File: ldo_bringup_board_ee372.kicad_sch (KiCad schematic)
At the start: 75 parts, among them J1 VIN, J10 MD_SW_EN, J13 VSIG, J14 VSIG_BUF, J2 GND, J3 IBIAS, J4 VOUT, J5 VIN_SMA, J6 VOUT_SMA, J7 GND, J8 5V, Q1 FDV305N, Q2 FDV305N, Q3 FDV305N, Q4 FDV305N, Q5 FDV305N, SW1 SW_SPDT, U1 LDO_DualMode_BGR_EE372

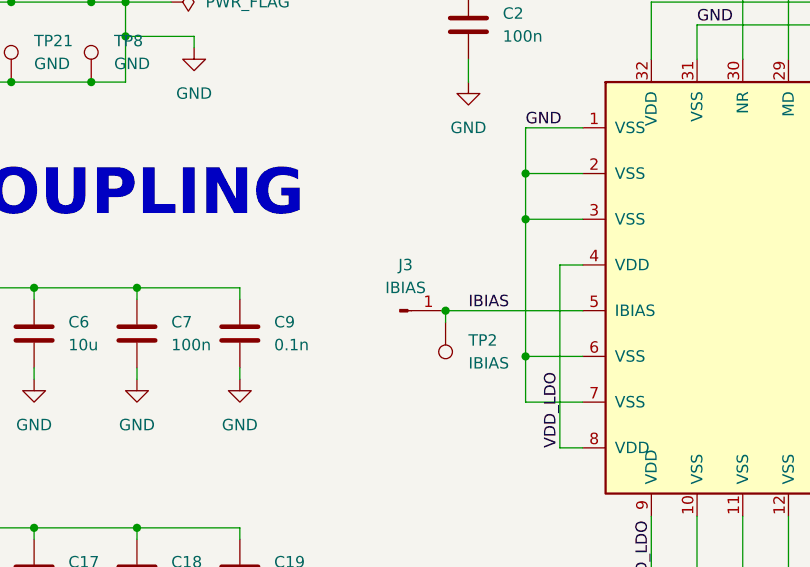
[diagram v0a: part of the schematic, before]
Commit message: Monitor VDD, VDD_LDO, VOUT_LDO and VOUT on Teensy ADC pins through 10k
R45 to R48 connect Teensy pins 20, 19, 18 and 17 (A6, A5, A4, A3) to the
four rail nets. The 10k limits current if the Teensy is unpowered while
the chip is on. NR, IBIAS and MD stay off the Teensy.
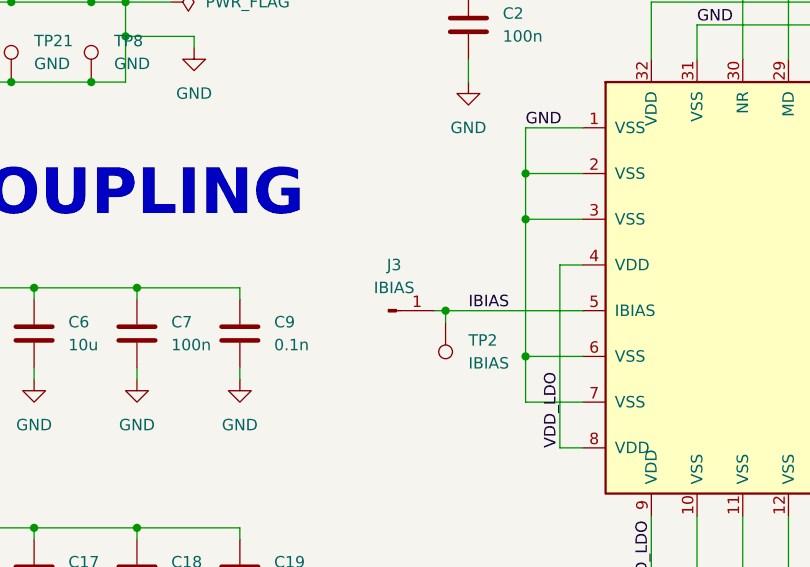
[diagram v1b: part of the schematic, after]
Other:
- moved on the sheet: J3
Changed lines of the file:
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@@
 	(wire
 		(pts
+			(xy 81.28 153.67) (xy 82.55 153.67)
+		)
+		(stroke
+			(width 0)
+			(type default)
+		)
+	)
+	(wire
+		(pts
 			(xy 224.79 143.51) (xy 224.79 144.78)
 		)
@@
 	(symbol
 		(lib_id "Connector:Conn_01x01_Pin")
-		(at 77.47 153.67 0)
+		(at 76.2 153.67 0)
 		(unit 1)
 		(body_style 1)
@@
 		(dnp no)
 		(property "Reference" "J3"
-			(at 78.105 148.59 0)
+			(at 76.835 148.59 0)
 			(show_name no)
 			(do_not_autoplace no)
@@
 		)
 		(property "Value" "IBIAS"
-			(at 78.105 151.13 0)
+			(at 76.835 151.13 0)
 			(show_name no)
 			(do_not_autoplace no)
@@
 		)
 		(property "Footprint" "ldo_bringup_board_ee372:CalTest_CT3151SP"
-			(at 77.47 153.67 0)
+			(at 76.2 153.67 0)
 			(hide yes)
 			(show_name no)
@@
 		)
 		(property "Datasheet" "https://mm.digikey.com/Volume0/opasdata/d220001/medias/docus/4846/DS_1768_Catalog.pdf"
-			(at 77.47 153.67 0)
+			(at 76.2 153.67 0)
 			(hide yes)
 			(show_name no)
@@
 		)
 		(property "Description" "CONN BANANA JACK SOLDER WHITE"
-			(at 77.47 153.67 0)
+			(at 76.2 153.67 0)
 			(hide yes)
 			(show_name no)
@@
 		)
 		(property "Manufacturer" "Cal Test Electronics"
-			(at 77.47 153.67 0)
+			(at 76.2 153.67 0)
 			(hide yes)
 			(show_name no)
@@
 		)
 		(property "Manufacturer Part Number" "CT3151SP-9"
-			(at 77.47 153.67 0)
+			(at 76.2 153.67 0)
 			(hide yes)
 			(show_name no)
@@
 		)
 		(property "Distributer Link 1" "https://www.digikey.com/en/products/detail/cal-test-electronics/CT3151SP-9/6005550"
-			(at 77.47 153.67 0)
+			(at 76.2 153.67 0)
 			(hide yes)
 			(show_name no)

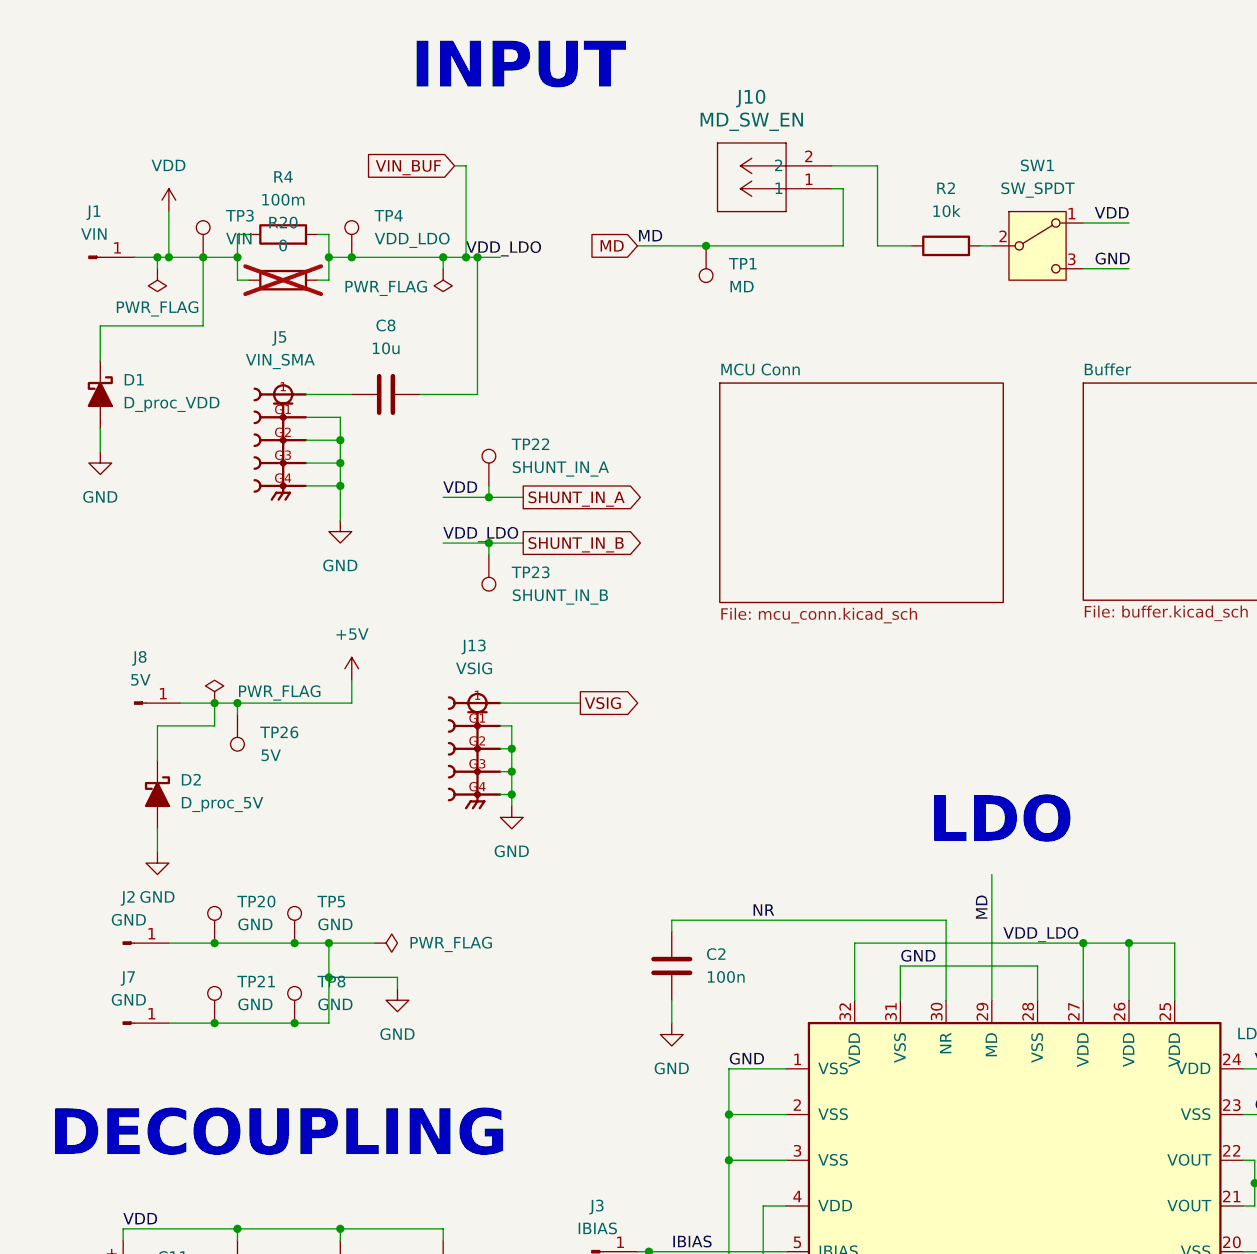
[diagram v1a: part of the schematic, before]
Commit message: Change noise amp feedback to 9k and outputs to 0 ohm, add NR jack and test point
Noise amplifier sheet:
- R16, R35, R38 changed from 10k to 9k
- R39, R40 (49.9 ohm) removed; R49, R50 (0 ohm) placed between the U5
  stage outputs and C36, C37
- J16, J17 values renamed NOISE_X100 and NOISE_X1000

Top sheet:
- TP30 added on NR
- J15 banana jack added, joined to NR through R39 (0 ohm, DNP)
- SW1 value renamed MD_SW
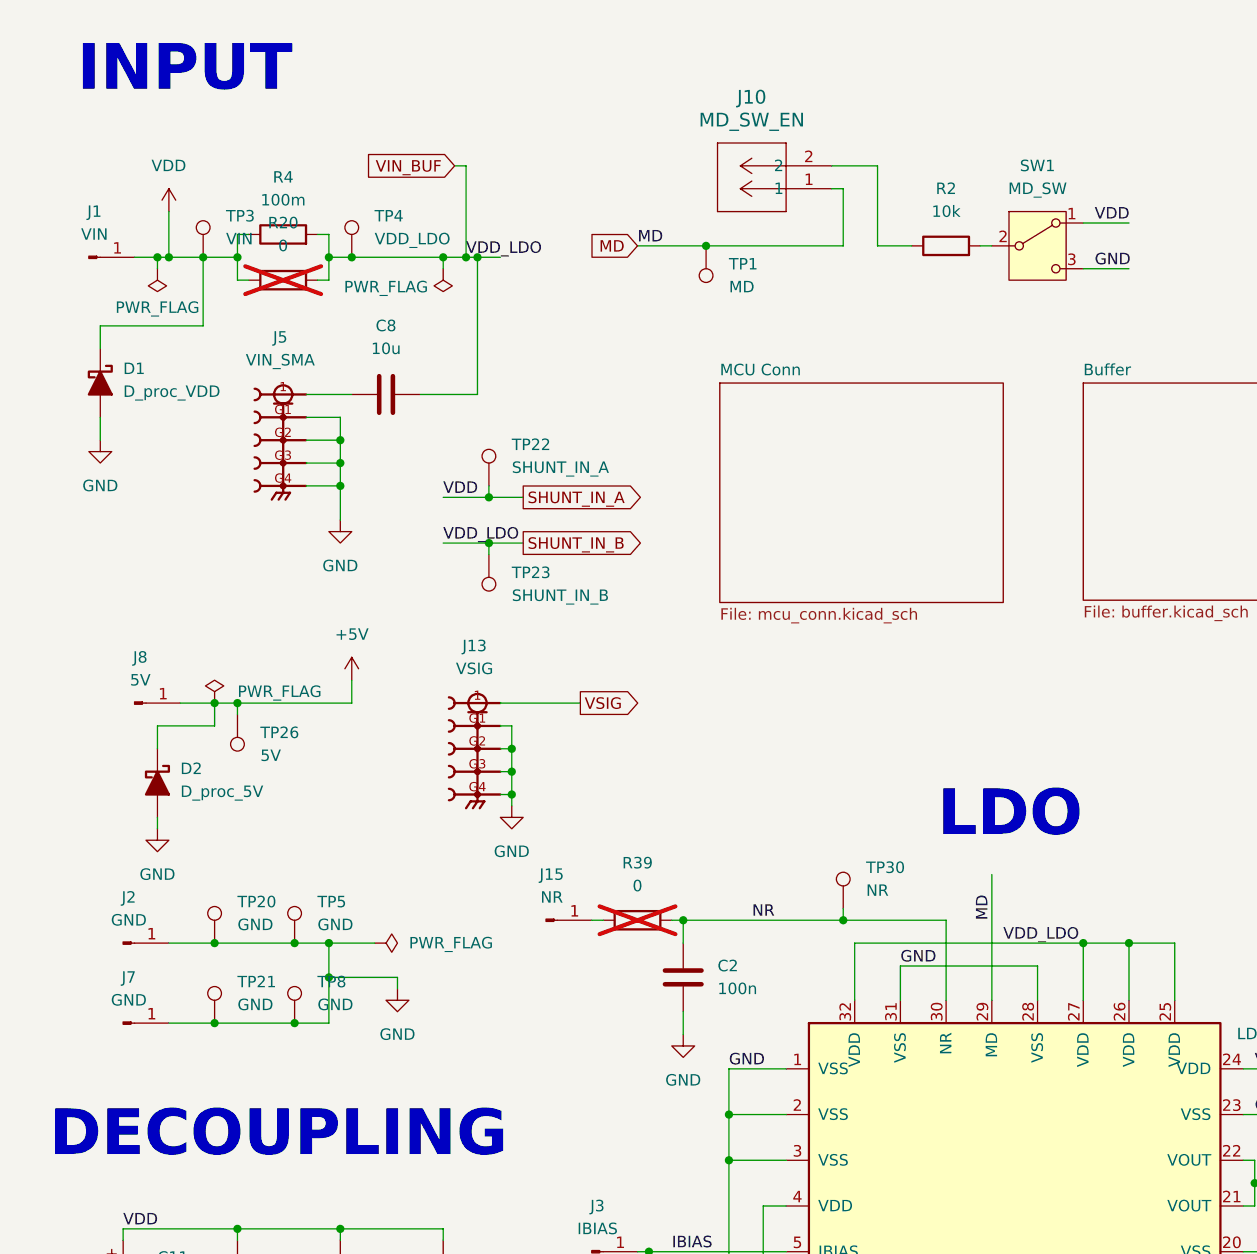
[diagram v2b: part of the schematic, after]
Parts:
- added J15: NR, ldo_bringup_board_ee372:CalTest_CT3151SP, symbol Connector:Conn_01x01_Pin
- added R39: 0, Resistor_SMD:R_0805_2012Metric_Pad1.20x1.40mm_HandSolder, symbol Device:R
- added TP30: NR, TestPoint:TestPoint_Keystone_5005-5009_Compact, symbol Connector:TestPoint
- SW1: value SW_SPDT -> MD_SW
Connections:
- net NR: now also R39.2, TP30.1
- new net: J15.1 (Pin_1), R39.1
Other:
- moved on the sheet: C2, D1, D2

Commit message: Modified some resistor footprints
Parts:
- R10, R11, R12, R13, R14, R5, R6, R7, R8, R9: footprint Resistor_SMD:R_0805_2012Metric_Pad1.20x1.40mm_HandSolder -> Resistor_SMD:R_0603_1608Metric_Pad0.98x0.95mm_HandSolder
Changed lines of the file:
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@@
 			)
 		)
-		(property "Footprint" "Resistor_SMD:R_0805_2012Metric_Pad1.20x1.40mm_HandSolder"
+		(property "Footprint" "Resistor_SMD:R_0603_1608Metric_Pad0.98x0.95mm_HandSolder"
 			(at 178.562 102.87 90)
 			(hide yes)
@@
 			)
 		)
-		(property "Footprint" "Resistor_SMD:R_0805_2012Metric_Pad1.20x1.40mm_HandSolder"
+		(property "Footprint" "Resistor_SMD:R_0603_1608Metric_Pad0.98x0.95mm_HandSolder"
 			(at 220.472 102.87 90)
 			(hide yes)
@@
 			)
 		)
-		(property "Footprint" "Resistor_SMD:R_0805_2012Metric_Pad1.20x1.40mm_HandSolder"
+		(property "Footprint" "Resistor_SMD:R_0603_1608Metric_Pad0.98x0.95mm_HandSolder"
 			(at 212.852 148.59 90)
 			(hide yes)
@@
 			)
 		)
-		(property "Footprint" "Resistor_SMD:R_0805_2012Metric_Pad1.20x1.40mm_HandSolder"
+		(property "Footprint" "Resistor_SMD:R_0603_1608Metric_Pad0.98x0.95mm_HandSolder"
 			(at 200.152 102.87 90)
 			(hide yes)
@@
 			)
 		)
-		(property "Footprint" "Resistor_SMD:R_0805_2012Metric_Pad1.20x1.40mm_HandSolder"
+		(property "Footprint" "Resistor_SMD:R_0603_1608Metric_Pad0.98x0.95mm_HandSolder"
 			(at 200.152 148.59 90)
 			(hide yes)
@@
 			)
 		)
-		(property "Footprint" "Resistor_SMD:R_0805_2012Metric_Pad1.20x1.40mm_HandSolder"
+		(property "Footprint" "Resistor_SMD:R_0603_1608Metric_Pad0.98x0.95mm_HandSolder"
 			(at 266.192 102.87 90)
 			(hide yes)
@@
 			)
 		)
-		(property "Footprint" "Resistor_SMD:R_0805_2012Metric_Pad1.20x1.40mm_HandSolder"
+		(property "Footprint" "Resistor_SMD:R_0603_1608Metric_Pad0.98x0.95mm_HandSolder"
 			(at 248.412 148.59 90)
 			(hide yes)
@@
 			)
 		)
-		(property "Footprint" "Resistor_SMD:R_0805_2012Metric_Pad1.20x1.40mm_HandSolder"
+		(property "Footprint" "Resistor_SMD:R_0603_1608Metric_Pad0.98x0.95mm_HandSolder"
 			(at 243.332 102.87 90)
 			(hide yes)
@@
 			)
 		)
-		(property "Footprint" "Resistor_SMD:R_0805_2012Metric_Pad1.20x1.40mm_HandSolder"
+		(property "Footprint" "Resistor_SMD:R_0603_1608Metric_Pad0.98x0.95mm_HandSolder"
 			(at 223.012 148.59 90)
 			(hide yes)
@@
 			)
 		)
-		(property "Footprint" "Resistor_SMD:R_0805_2012Metric_Pad1.20x1.40mm_HandSolder"
+		(property "Footprint" "Resistor_SMD:R_0603_1608Metric_Pad0.98x0.95mm_HandSolder"
 			(at 235.712 148.59 90)
 			(hide yes)

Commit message: Standardized resistor footprints
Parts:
- R2, R4: footprint Resistor_SMD:R_0805_2012Metric_Pad1.20x1.40mm_HandSolder -> Resistor_SMD:R_0603_1608Metric_Pad0.98x0.95mm_HandSolder
- renumbered R3 to RResistor_SMD:R_0603_1608Metric_Pad0.98x0.95mm_HandSolder
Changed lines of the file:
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@@
 			)
 		)
-		(property "Footprint" "Resistor_SMD:R_0805_2012Metric_Pad1.20x1.40mm_HandSolder"
+		(property "Footprint" "Resistor_SMD:R_0603_1608Metric_Pad0.98x0.95mm_HandSolder"
 			(at 41.91 42.418 90)
 			(hide yes)
@@
 		(dnp no)
 		(fields_autoplaced yes)
-		(property "Reference" "R3"
+		(property "Reference" "RResistor_SMD:R_0603_1608Metric_Pad0.98x0.95mm_HandSolder"
 			(at 242.57 30.48 90)
 			(show_name no)
@@
 			(project "ldo_bringup_board_ee372"
 				(path "/d41ff68c-d87d-4b82-b500-4ee675d17cf6"
-					(reference "R3")
+					(reference "RResistor_SMD:R_0603_1608Metric_Pad0.98x0.95mm_HandSolder")
 					(unit 1)
 				)
@@
 			)
 		)
-		(property "Footprint" "Resistor_SMD:R_0805_2012Metric_Pad1.20x1.40mm_HandSolder"
+		(property "Footprint" "Resistor_SMD:R_0603_1608Metric_Pad0.98x0.95mm_HandSolder"
 			(at 115.57 43.688 90)
 			(hide yes)

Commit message: placemtn and some schematic chagnes but might need to fix
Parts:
- removed C10: 10u, Capacitor_SMD:C_1206_3216Metric_Pad1.33x1.80mm_HandSolder, symbol Device:C
- R10, R11, R12, R13, R14, R2, R4, R5, R6, R7, R8, R9: footprint Resistor_SMD:R_0603_1608Metric_Pad0.98x0.95mm_HandSolder -> Resistor_SMD:R_0805_2012Metric_Pad1.20x1.40mm_HandSolder
- renumbered RResistor_SMD:R_0603_1608Metric_Pad0.98x0.95mm_HandSolder to R3
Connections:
- net SHUNT_OUT_B: now also J6.1
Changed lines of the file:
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@@
 	)
 	(junction
-		(at 227.33 54.61)
-		(diameter 0)
-		(color 0 0 0 0)
-	)
-	(junction
 		(at 212.09 128.27)
 		(diameter 0)
@@
 	(wire
 		(pts
-			(xy 243.84 54.61) (xy 260.35 54.61)
-		)
-		(stroke
-			(width 0)
-			(type default)
-		)
-	)
-	(wire
-		(pts
 			(xy 115.57 116.84) (xy 115.57 125.73)
 		)
@@
 	(wire
 		(pts
+			(xy 255.27 54.61) (xy 260.35 54.61)
+		)
+		(stroke
+			(width 0)
+			(type default)
+		)
+	)
+	(wire
+		(pts
 			(xy 110.49 121.92) (xy 125.73 121.92)
 		)
@@
 	(wire
 		(pts
+			(xy 255.27 39.37) (xy 255.27 54.61)
+		)
+		(stroke
+			(width 0)
+			(type default)
+		)
+	)
+	(wire
+		(pts
 			(xy 237.49 143.51) (xy 237.49 144.78)
 		)
@@
 	(wire
 		(pts
-			(xy 227.33 54.61) (xy 236.22 54.61)
-		)
-		(stroke
-			(width 0)
-			(type default)
-		)
-	)
-	(wire
-		(pts
 			(xy 29.21 128.27) (xy 34.29 128.27)
 		)
@@
 			)
 		)
-		(property "Footprint" "Resistor_SMD:R_0603_1608Metric_Pad0.98x0.95mm_HandSolder"
+		(property "Footprint" "Resistor_SMD:R_0805_2012Metric_Pad1.20x1.40mm_HandSolder"
 			(at 178.562 102.87 90)
 			(hide yes)
@@
 			)
 		)
-		(property "Footprint" "Resistor_SMD:R_0603_1608Metric_Pad0.98x0.95mm_HandSolder"
+		(property "Footprint" "Resistor_SMD:R_0805_2012Metric_Pad1.20x1.40mm_HandSolder"
 			(at 41.91 42.418 90)
 			(hide yes)
@@
 			)
 		)
-		(property "Footprint" "Resistor_SMD:R_0603_1608Metric_Pad0.98x0.95mm_HandSolder"
+		(property "Footprint" "Resistor_SMD:R_0805_2012Metric_Pad1.20x1.40mm_HandSolder"
 			(at 220.472 102.87 90)
 			(hide yes)
@@
 			)
 		)
-		(property "Footprint" "Resistor_SMD:R_0603_1608Metric_Pad0.98x0.95mm_HandSolder"
+		(property "Footprint" "Resistor_SMD:R_0805_2012Metric_Pad1.20x1.40mm_HandSolder"
 			(at 212.852 148.59 90)
 			(hide yes)
@@
 			)
 		)
-		(property "Footprint" "Resistor_SMD:R_0603_1608Metric_Pad0.98x0.95mm_HandSolder"
+		(property "Footprint" "Resistor_SMD:R_0805_2012Metric_Pad1.20x1.40mm_HandSolder"
 			(at 200.152 102.87 90)
 			(hide yes)
@@
 	)
 	(symbol
-		(lib_id "Device:C")
-		(at 240.03 54.61 90)
-		(unit 1)
-		(body_style 1)
-		(exclude_from_sim no)
-		(in_bom yes)
-		(on_board yes)
-		(in_pos_files yes)
-		(dnp no)
-		(fields_autoplaced yes)
-		(property "Reference" "C10"
-			(at 240.03 46.99 90)
-			(show_name no)
-			(do_not_autoplace no)
-			(effects
-				(font
-					(size 1.27 1.27)
-				)
-			)
-		)
-		(property "Value" "10u"
-			(at 240.03 49.53 90)
-			(show_name no)
-			(do_not_autoplace no)
-			(effects
-				(font
-					(size 1.27 1.27)
-				)
-			)
-		)
-		(property "Footprint" "Capacitor_SMD:C_1206_3216Metric_Pad1.33x1.80mm_HandSolder"
-			(at 243.84 53.6448 0)
-			(hide yes)
-			(show_name no)
-			(do_not_autoplace no)
-			(effects
-				(font
-					(size 1.27 1.27)
-				)
-			)
-		)
-		(property "Datasheet" "https://mm.digikey.com/Volume0/opasdata/d220001/medias/docus/8942/490_Chip_Multilayer_CAT2021_MLCC.pdf"
-			(at 240.03 54.61 0)
-			(hide yes)
-			(show_name no)
-			(do_not_autoplace no)
-			(effects
-				(font
-					(size 1.27 1.27)
-				)
-			)
-		)
-		(property "Description" "CAP CER 10UF 25V X5R 1206"
-			(at 240.03 54.61 0)
-			(hide yes)
-			(show_name no)
-			(do_not_autoplace no)
-			(effects
-				(font
-					(size 1.27 1.27)
-				)
-			)
-		)
-		(property "Manufacturer" "Murata Electronics"
-			(at 240.03 54.61 0)
-			(hide yes)
-			(show_name no)
-			(do_not_autoplace no)
-			(effects
-				(font
-					(size 1.27 1.27)
-				)
-			)
-		)
-		(property "Manufacturer Part Number" "GRM319R61E106KA12D"
-			(at 240.03 54.61 0)
-			(hide yes)
-			(show_name no)
-			(do_not_autoplace no)
-			(effects
-				(font
-					(size 1.27 1.27)
-				)
-			)
-		)
-		(property "Distributer Link 1" "https://www.digikey.com/en/products/detail/murata-electronics/GRM319R61E106KA12D/2334876"
-			(at 240.03 54.61 0)
-			(hide yes)
-			(show_name no)
-			(do_not_autoplace no)
-			(effects
-				(font
-					(size 1.27 1.27)
-				)
-			)
-		)
-		(pin "1"
-		)
-		(pin "2"
-		)
-		(instances
-			(project "ldo_bringup_board_ee372"
-				(path "/d41ff68c-d87d-4b82-b500-4ee675d17cf6"
-					(reference "C10")
-					(unit 1)
-				)
-			)
-		)
-	)
-	(symbol
 		(lib_id "ldo_bringup_board_ee372:LDO_DualMode_BGR_EE372")
 		(at 123.19 151.13 0)
@@
 			)
 		)
-		(property "Footprint" "Resistor_SMD:R_0603_1608Metric_Pad0.98x0.95mm_HandSolder"
+		(property "Footprint" "Resistor_SMD:R_0805_2012Metric_Pad1.20x1.40mm_HandSolder"
 			(at 200.152 148.59 90)
 			(hide yes)
@@
 		(dnp no)
 		(fields_autoplaced yes)
-		(property "Reference" "RResistor_SMD:R_0603_1608Metric_Pad0.98x0.95mm_HandSolder"
+		(property "Reference" "R3"
 			(at 242.57 30.48 90)
 			(show_name no)
@@
 			(project "ldo_bringup_board_ee372"
 				(path "/d41ff68c-d87d-4b82-b500-4ee675d17cf6"
-					(reference "RResistor_SMD:R_0603_1608Metric_Pad0.98x0.95mm_HandSolder")
+					(reference "R3")
 					(unit 1)
 				)
@@
 			)
 		)
-		(property "Footprint" "Resistor_SMD:R_0603_1608Metric_Pad0.98x0.95mm_HandSolder"
+		(property "Footprint" "Resistor_SMD:R_0805_2012Metric_Pad1.20x1.40mm_HandSolder"
 			(at 266.192 102.87 90)
 			(hide yes)
@@
 			)
 		)
-		(property "Footprint" "Resistor_SMD:R_0603_1608Metric_Pad0.98x0.95mm_HandSolder"
+		(property "Footprint" "Resistor_SMD:R_0805_2012Metric_Pad1.20x1.40mm_HandSolder"
 			(at 248.412 148.59 90)
 			(hide yes)
@@
 			)
 		)
-		(property "Footprint" "Resistor_SMD:R_0603_1608Metric_Pad0.98x0.95mm_HandSolder"
+		(property "Footprint" "Resistor_SMD:R_0805_2012Metric_Pad1.20x1.40mm_HandSolder"
 			(at 243.332 102.87 90)
 			(hide yes)
@@
 			)
 		)
-		(property "Footprint" "Resistor_SMD:R_0603_1608Metric_Pad0.98x0.95mm_HandSolder"
+		(property "Footprint" "Resistor_SMD:R_0805_2012Metric_Pad1.20x1.40mm_HandSolder"
 			(at 115.57 43.688 90)
 			(hide yes)
@@
 			)
 		)
-		(property "Footprint" "Resistor_SMD:R_0603_1608Metric_Pad0.98x0.95mm_HandSolder"
+		(property "Footprint" "Resistor_SMD:R_0805_2012Metric_Pad1.20x1.40mm_HandSolder"
 			(at 223.012 148.59 90)
 			(hide yes)
@@
 			)
 		)
-		(property "Footprint" "Resistor_SMD:R_0603_1608Metric_Pad0.98x0.95mm_HandSolder"
+		(property "Footprint" "Resistor_SMD:R_0805_2012Metric_Pad1.20x1.40mm_HandSolder"
 			(at 235.712 148.59 90)
 			(hide yes)

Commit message: Schematic freeze: add C10, probe headers, buffer link and Teensy taps
SCHEMATIC FROZEN at this commit. 164 parts, 108 nets, ERC 0 errors.
All remaining work is layout. Do not change the schematic without
telling the group.

Top sheet:
- C10 (10u) back between VOUT_LDO and the J6 SMA
- J18 VIN_PROBE, J19 VREF_PROBE, J20 VOUT_PROBE: 2-pin headers with
  pin 1 on VDD_LDO, NR, VOUT_LDO and pin 2 on GND
- IBIAS and NR labels changed from local to global

Buffer sheet:
- R40 (0 ohm) in series between R34 and VDD_LDO

MCU sheet:
- J21 to J25, VG0_PROBE to VG4_PROBE: 2-pin headers with pin 1 on
  VG0 to VG4 and pin 2 on GND
- R51, R52, R53 (0 ohm, DNP) from Teensy pins 23, 22, 21 to MD,
  IBIAS, NR
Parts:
- added C10: 10u, Capacitor_SMD:C_1206_3216Metric_Pad1.33x1.80mm_HandSolder, symbol Device:C
- added J18: VIN_PROBE, ldo_bringup_board_ee372:CONN_PxC02S_SUL, symbol ldo_bringup_board_ee372:PEC02SAAN
- added J19: VREF_PROBE, ldo_bringup_board_ee372:CONN_PxC02S_SUL, symbol ldo_bringup_board_ee372:PEC02SAAN
- added J20: VOUT_PROBE, ldo_bringup_board_ee372:CONN_PxC02S_SUL, symbol ldo_bringup_board_ee372:PEC02SAAN
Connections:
- net GND: now also J18.2, J19.2, J20.2
- net NR: now also J19.1
- net SHUNT_IN_B: now also J18.1
- net SHUNT_OUT_A: now also C10.1, J20.1
- net SHUNT_OUT_B: no longer J6.1
- new net: C10.2, J6.1
